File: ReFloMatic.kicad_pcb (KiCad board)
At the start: 2 copper layers, 39 parts, among them CON2 MicroSD_Card, P1 PROG, P2 THERMOCOUPLE, P3 DOOR_SERVO, P4 OVEN, P5 USB_B, Q1 MMUN2211, Q2 MMUN2111, Q3 MMUN2111, Q4 MMUN2211, U1 STM32F030C, U2 MAX31855KASA

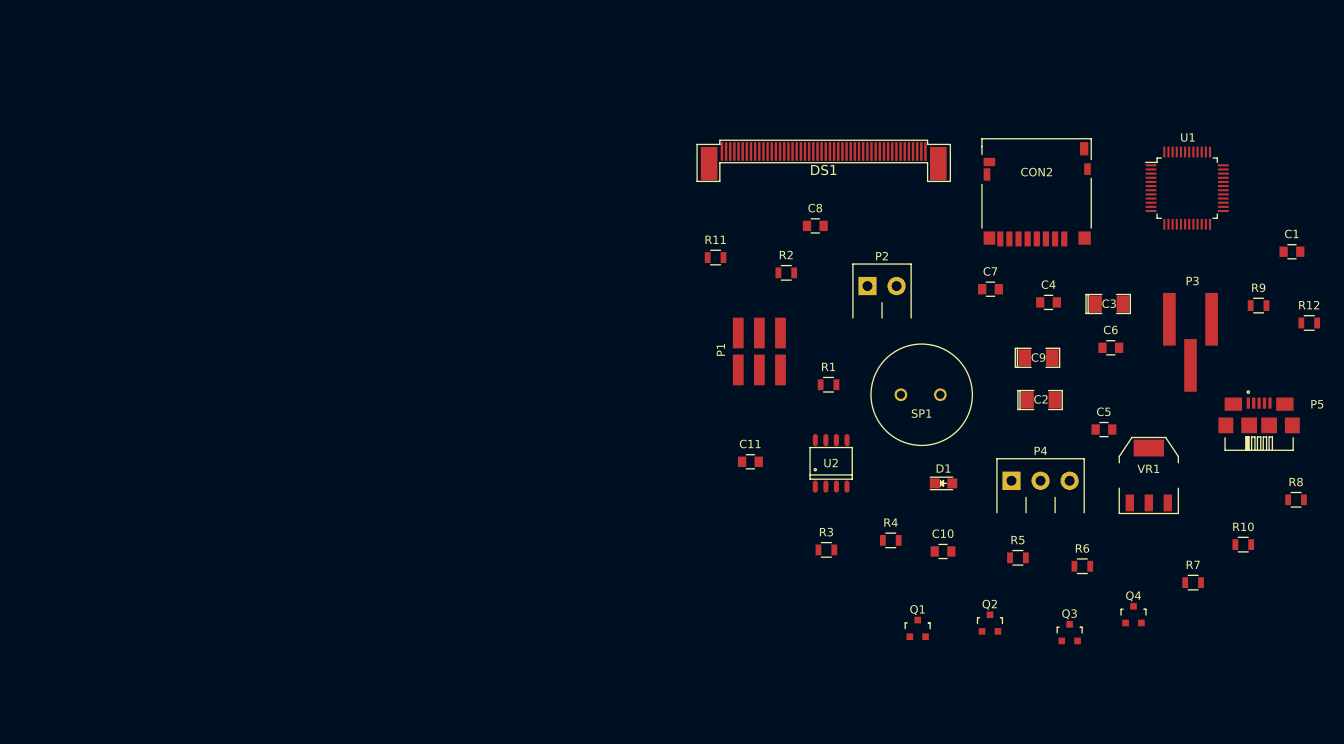
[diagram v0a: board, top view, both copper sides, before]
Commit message: Added TFT footprint that contains display and PCB cutout.
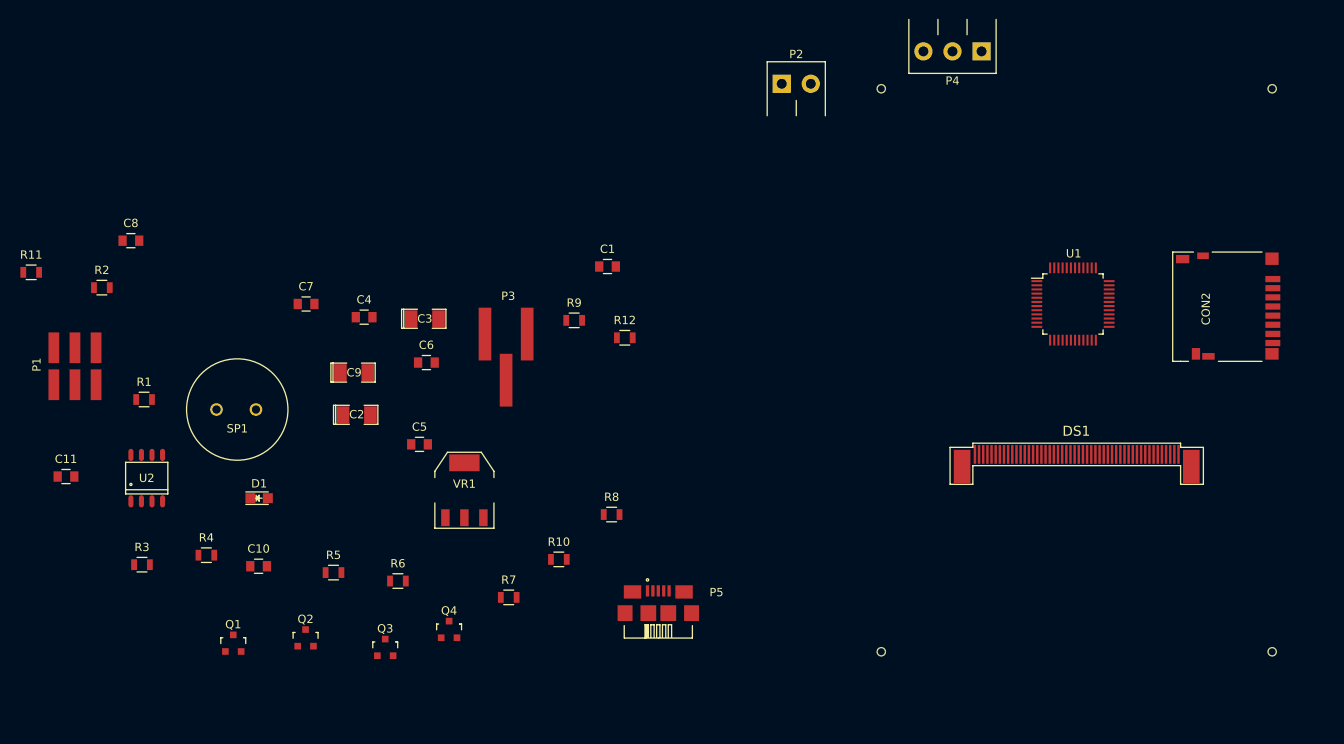
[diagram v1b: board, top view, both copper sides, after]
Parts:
- DS1: footprint TFT:FPC_50 -> TFT:ER-TFT028-4
- moved C4 82.4 mm to (67.5, 99.2)
- moved C6 82.4 mm to (75.0, 104.6)
- moved C9 82.4 mm to (66.3, 105.9)
- moved Q3 82.4 mm to (70.0, 138.9)
- moved R10 82.4 mm to (90.9, 128.3)
- moved R12 82.4 mm to (98.9, 101.7)
- moved R6 82.4 mm to (71.6, 130.9)
- moved R8 82.4 mm to (97.3, 122.9)
- moved R9 82.4 mm to (92.8, 99.6)
- moved VR1 82.4 mm to (79.6, 120.0)
- moved C10 82.4 mm to (54.8, 129.2)
- moved C11 82.4 mm to (31.6, 118.4)
- moved C2 82.4 mm to (66.6, 110.9)
- moved C3 82.4 mm to (74.8, 99.4)
- moved C5 82.4 mm to (74.2, 114.5)
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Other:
- net class Default: clearance 0.2 -> 0.1524; trace_width 0.25 -> 0.1524; via_dia 0.6 -> 0.6858; via_drill 0.4 -> 0.3302
- rule trace_clearance: 0.2 -> 0.1524
- rule trace_min: 0.2 -> 0.1524
- rule via_min_drill: 0.3 -> 0.3302
- rule via_min_size: 0.4 -> 0.6858

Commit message: Preliminary component placement.
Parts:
- added P6: PWR_CONN, Pin_Headers:Pin_Header_Straight_1x02, F.Cu at (153.5, 144.7)
- added REF**: MountingHole_3mm, Mounting_Holes:MountingHole_3mm, F.Cu at (176.5, 144.9)
- added REF**: MountingHole_3mm, Mounting_Holes:MountingHole_3mm, F.Cu at (129.9, 144.7)
- added REF**: MountingHole_3mm, Mounting_Holes:MountingHole_3mm, F.Cu at (129.9, 66.8)
- added REF**: MountingHole_3mm, Mounting_Holes:MountingHole_3mm, F.Cu at (176.5, 66.8)
- P3: footprint Connectors-Custom3:HEADER_1X3_SMD -> Pin_Headers:Pin_Header_Straight_1x03
- moved R11 149.6 mm to (177.0, 93.3)
- moved R2 139.7 mm to (174.0, 74.7)
- moved R1 132.6 mm to (169.1, 74.9)
- moved C11 132.0 mm to (163.6, 120.7), turned to 270 degrees
- moved U2 131.9 mm to (168.4, 83.3), turned to 180 degrees
- moved P1 126.3 mm to (157.3, 85.0), turned to 180 degrees
- moved D1 116.7 mm to (171.0, 132.5), turned to 180 degrees
- moved R3 107.6 mm to (140.4, 88.4)
- moved C10 106.8 mm to (161.2, 120.7), turned to 270 degrees
- moved R4 106.0 mm to (141.0, 76.0)
- moved C8 103.8 mm to (141.2, 110.4)
- moved Q3 103.3 mm to (150.8, 74.6)
- moved Q2 102.5 mm to (144.6, 79.1)
- moved R5 99.4 mm to (145.6, 73.3)
- moved C7 95.4 mm to (155.4, 106.9)
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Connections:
- VR1 pad 4: (no net) -> +3V3
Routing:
- added copper zone on F.Cu, net +3V3
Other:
- board outline added: 54.4 x 85.3 mm

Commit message: Began routing.
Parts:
- added REF**11111: VIA-27mil, Miscellanious:VIA-27mil, F.Cu at (144.9, 139.9)
- added REF**11111: VIA-27mil, Miscellanious:VIA-27mil, F.Cu at (153.3, 138.9)
- added REF**11112: VIA-27mil, Miscellanious:VIA-27mil, F.Cu at (144.9, 140.9)
- added REF**11112: VIA-27mil, Miscellanious:VIA-27mil, F.Cu at (153.3, 140.0)
- added REF**11113: VIA-27mil, Miscellanious:VIA-27mil, F.Cu at (144.9, 142.0)
- added REF**11113: VIA-27mil, Miscellanious:VIA-27mil, F.Cu at (153.3, 141.0)
- added REF**11114: VIA-27mil, Miscellanious:VIA-27mil, F.Cu at (144.9, 143.0)
- added REF**11114: VIA-27mil, Miscellanious:VIA-27mil, F.Cu at (153.3, 142.0)
- added REF**11121: VIA-27mil, Miscellanious:VIA-27mil, F.Cu at (145.9, 139.9)
- added REF**11121: VIA-27mil, Miscellanious:VIA-27mil, F.Cu at (154.3, 138.9)
- added REF**11122: VIA-27mil, Miscellanious:VIA-27mil, F.Cu at (145.9, 140.9)
- added REF**11122: VIA-27mil, Miscellanious:VIA-27mil, F.Cu at (154.3, 140.0)
- added REF**11123: VIA-27mil, Miscellanious:VIA-27mil, F.Cu at (145.9, 142.0)
- added REF**11123: VIA-27mil, Miscellanious:VIA-27mil, F.Cu at (154.3, 141.0)
- added REF**11124: VIA-27mil, Miscellanious:VIA-27mil, F.Cu at (145.9, 143.0)
- added REF**11124: VIA-27mil, Miscellanious:VIA-27mil, F.Cu at (154.3, 142.0)
- added REF**11131: VIA-27mil, Miscellanious:VIA-27mil, F.Cu at (146.9, 139.9)
- added REF**11131: VIA-27mil, Miscellanious:VIA-27mil, F.Cu at (155.3, 138.9)
- added REF**11132: VIA-27mil, Miscellanious:VIA-27mil, F.Cu at (146.9, 140.9)
- added REF**11132: VIA-27mil, Miscellanious:VIA-27mil, F.Cu at (155.3, 140.0)
- added REF**11133: VIA-27mil, Miscellanious:VIA-27mil, F.Cu at (146.9, 142.0)
- added REF**11133: VIA-27mil, Miscellanious:VIA-27mil, F.Cu at (155.3, 141.0)
- added REF**11134: VIA-27mil, Miscellanious:VIA-27mil, F.Cu at (146.9, 143.0)
- added REF**11134: VIA-27mil, Miscellanious:VIA-27mil, F.Cu at (155.3, 142.0)
- added REF**11141: VIA-27mil, Miscellanious:VIA-27mil, F.Cu at (148.0, 139.9)
- added REF**11141: VIA-27mil, Miscellanious:VIA-27mil, F.Cu at (156.4, 138.9)
- added REF**11142: VIA-27mil, Miscellanious:VIA-27mil, F.Cu at (148.0, 140.9)
- added REF**11142: VIA-27mil, Miscellanious:VIA-27mil, F.Cu at (156.4, 140.0)
- added REF**11143: VIA-27mil, Miscellanious:VIA-27mil, F.Cu at (148.0, 142.0)
- added REF**11143: VIA-27mil, Miscellanious:VIA-27mil, F.Cu at (156.4, 141.0)
- added REF**11144: VIA-27mil, Miscellanious:VIA-27mil, F.Cu at (148.0, 143.0)
- added REF**11144: VIA-27mil, Miscellanious:VIA-27mil, F.Cu at (156.4, 142.0)
- moved C6 22.2 mm to (135.7, 103.2), turned to 180 degrees
- moved C4 20.4 mm to (141.8, 110.9), turned to 270 degrees
- moved C5 20.1 mm to (139.5, 110.9), turned to 270 degrees
- moved R2 12.9 mm to (161.2, 73.1), turned to 90 degrees
- moved C8 11.0 mm to (135.6, 100.9), turned to 180 degrees
- moved Q3 10.7 mm to (140.1, 75.2), turned to 90 degrees
- moved R5 7.09 mm to (138.6, 71.9)
- moved C1 6.76 mm to (169.3, 78.1)
- moved R4 6.36 mm to (146.0, 72.0)
- moved R3 6.36 mm to (134.3, 90.2), turned to 180 degrees
- moved R1 4.49 mm to (165.0, 73.0), turned to 90 degrees
- moved Q2 4.03 mm to (144.9, 75.1)
- moved C7 3.91 mm to (155.4, 103.0)
- moved Q1 3.88 mm to (138.1, 90.8)
- moved P1 2.49 mm to (154.8, 85.1), turned to 0 degrees
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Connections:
- DS1 pad 0: (no net) -> GND
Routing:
- net +3V3: track 0.00 -> 291.3 mm, vias 0 -> 4
- net GND: track 0.00 -> 47.9 mm, vias 0 -> 4
- net +5V: track 0.00 -> 40.6 mm
- net Net-(DS1-Pad5): track 0.00 -> 16.9 mm
- net Net-(C1-Pad2): track 0.00 -> 14.9 mm, vias 0 -> 2
- net Net-(DS1-Pad4): track 0.00 -> 14.3 mm
- net Net-(Q1-Pad3): track 0.00 -> 11.7 mm
- net Net-(DS1-Pad3): track 0.00 -> 11.5 mm
- net Net-(C1-Pad1): track 0.00 -> 10.2 mm
- net Net-(DS1-Pad2): track 0.00 -> 9.81 mm
- net Net-(P4-Pad2): track 0.00 -> 5.64 mm
- net Net-(P4-Pad1): track 0.00 -> 5.56 mm
- net Net-(P2-Pad1): track 0.00 -> 5.02 mm
- net Net-(P2-Pad2): track 0.00 -> 4.97 mm
- net Net-(D1-Pad1): track 0.00 -> 4.85 mm, vias 0 -> 2
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- added copper zone on B.Cu, net GND
- added copper zone on F.Cu, net GND
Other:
- net class Default: clearance 0.1524 -> 0.254; trace_width 0.1524 -> 0.508
- rule trace_clearance: 0.1524 -> 0.254

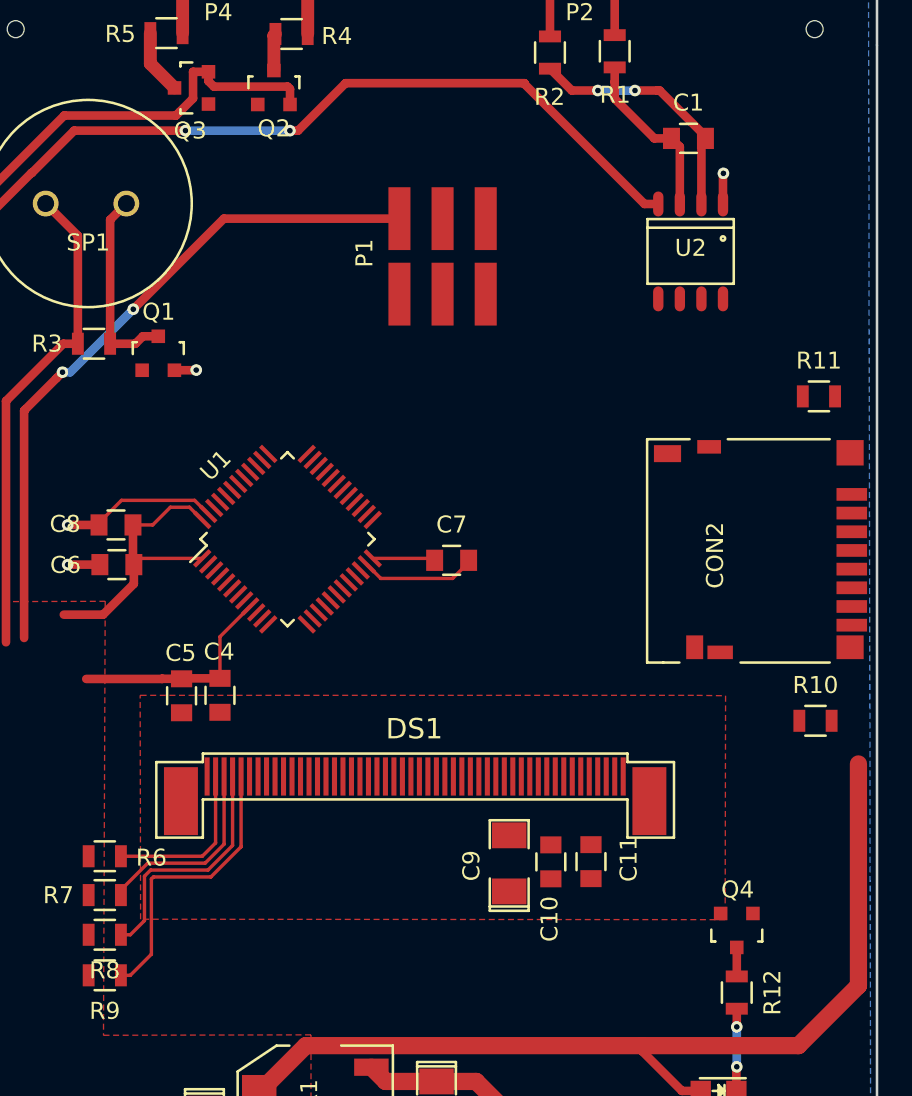
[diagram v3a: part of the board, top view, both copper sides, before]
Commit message: Routing mostly done.  Still need to route TFT traces.
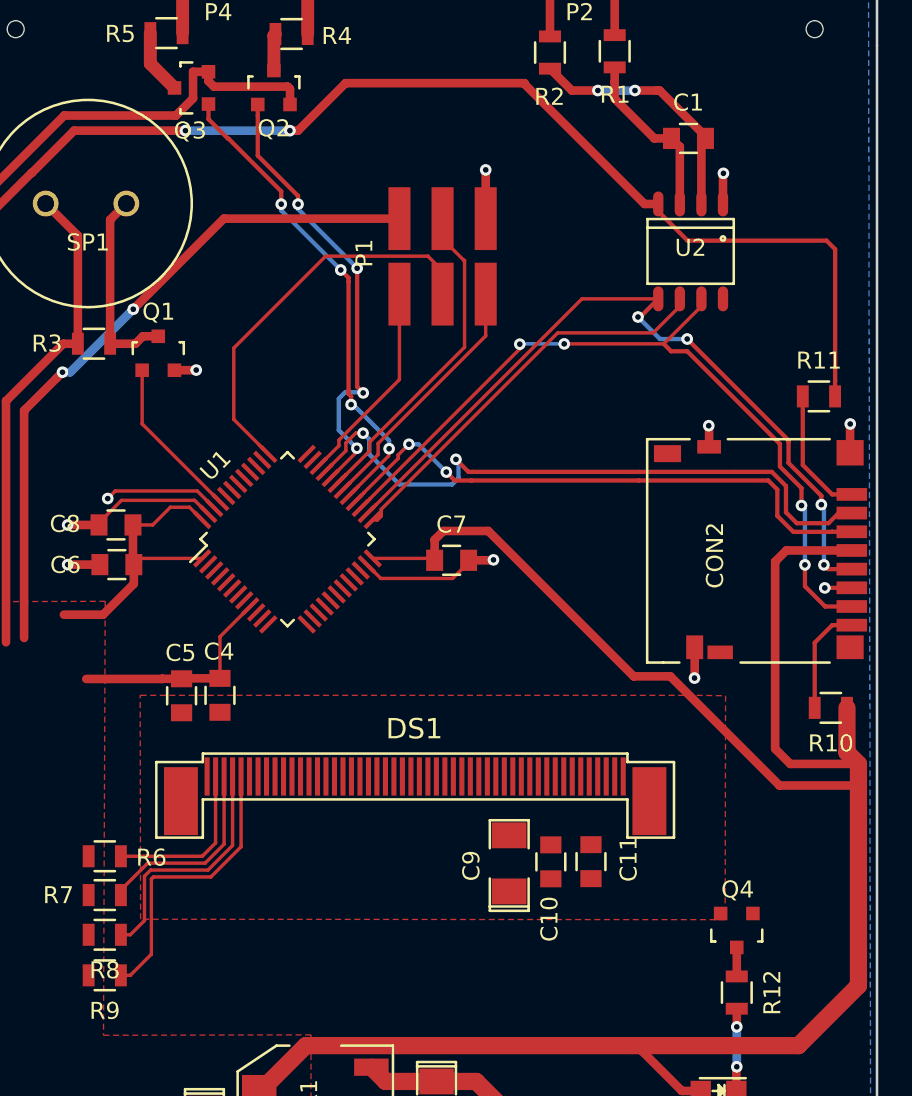
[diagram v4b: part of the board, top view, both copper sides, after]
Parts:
- moved R10 1.18 mm to (177.7, 111.7), turned to 180 degrees
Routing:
- net +3V3: track 291.3 -> 368.9 mm
- net /MAX_SD_MISO: track 0.00 -> 47.1 mm, vias 0 -> 4
- net /MAX_SD_SCK: track 0.00 -> 45.9 mm, vias 0 -> 4
- net /~SD_CS: track 0.00 -> 38.2 mm, vias 0 -> 2
- net /SD_MOSI: track 0.00 -> 33.8 mm, vias 0 -> 2
- net /OVEN2: track 0.00 -> 28.6 mm, vias 0 -> 4
- net /OVEN1: track 0.00 -> 26.9 mm, vias 0 -> 4
- net /~MAX_CS: track 0.00 -> 24.0 mm
- net /SWCLK: track 0.00 -> 23.3 mm
- net /UART_RX: track 0.00 -> 20.1 mm
- net /UART_TX: track 0.00 -> 15.0 mm
- net /SWDIO: track 0.00 -> 12.1 mm
- net GND: track 47.9 -> 58.6 mm, vias 4 -> 10
- net /BUZZER: track 0.00 -> 9.66 mm
- net Net-(CON2-Pad1): track 0.00 -> 7.64 mm
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
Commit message: Finished layout.
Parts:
- added REF**1111111: VIA-27mil, Miscellanious:VIA-27mil, F.Cu at (165.8, 138.4)
- added REF**1111111: VIA-27mil, Miscellanious:VIA-27mil, F.Cu at (138.1, 113.2)
- added REF**1111112: VIA-27mil, Miscellanious:VIA-27mil, F.Cu at (165.8, 139.4)
- added REF**1111112: VIA-27mil, Miscellanious:VIA-27mil, F.Cu at (138.1, 114.2)
- added REF**1111113: VIA-27mil, Miscellanious:VIA-27mil, F.Cu at (165.8, 140.5)
- added REF**1111121: VIA-27mil, Miscellanious:VIA-27mil, F.Cu at (166.8, 138.4)
- added REF**1111121: VIA-27mil, Miscellanious:VIA-27mil, F.Cu at (139.1, 113.2)
- added REF**1111122: VIA-27mil, Miscellanious:VIA-27mil, F.Cu at (166.8, 139.4)
- added REF**1111122: VIA-27mil, Miscellanious:VIA-27mil, F.Cu at (139.1, 114.2)
- added REF**1111123: VIA-27mil, Miscellanious:VIA-27mil, F.Cu at (166.8, 140.5)
- added REF**1111131: VIA-27mil, Miscellanious:VIA-27mil, F.Cu at (167.8, 138.4)
- added REF**1111131: VIA-27mil, Miscellanious:VIA-27mil, F.Cu at (140.2, 113.2)
- added REF**11111311: VIA-27mil, Miscellanious:VIA-27mil, F.Cu at (146.7, 112.0)
- added REF**111113111: VIA-27mil, Miscellanious:VIA-27mil, F.Cu at (165.2, 111.7)
- added REF**1111131111: VIA-27mil, Miscellanious:VIA-27mil, F.Cu at (146.2, 118.7)
- added REF**1111131112: VIA-27mil, Miscellanious:VIA-27mil, F.Cu at (146.2, 119.9)
- added REF**1111131113: VIA-27mil, Miscellanious:VIA-27mil, F.Cu at (146.2, 121.2)
- added REF**1111131114: VIA-27mil, Miscellanious:VIA-27mil, F.Cu at (146.2, 122.5)
- added REF**111113112: VIA-27mil, Miscellanious:VIA-27mil, F.Cu at (165.2, 112.7)
- added REF**1111131121: VIA-27mil, Miscellanious:VIA-27mil, F.Cu at (147.5, 118.7)
- added REF**1111131122: VIA-27mil, Miscellanious:VIA-27mil, F.Cu at (147.5, 119.9)
- added REF**1111131123: VIA-27mil, Miscellanious:VIA-27mil, F.Cu at (147.5, 121.2)
- added REF**1111131124: VIA-27mil, Miscellanious:VIA-27mil, F.Cu at (147.5, 122.5)
- added REF**111113113: VIA-27mil, Miscellanious:VIA-27mil, F.Cu at (165.2, 113.7)
- added REF**1111131131: VIA-27mil, Miscellanious:VIA-27mil, F.Cu at (148.7, 118.7)
- added REF**1111131132: VIA-27mil, Miscellanious:VIA-27mil, F.Cu at (148.7, 119.9)
- added REF**1111131133: VIA-27mil, Miscellanious:VIA-27mil, F.Cu at (148.7, 121.2)
- added REF**1111131134: VIA-27mil, Miscellanious:VIA-27mil, F.Cu at (148.7, 122.5)
- added REF**1111131141: VIA-27mil, Miscellanious:VIA-27mil, F.Cu at (150.0, 118.7)
- added REF**1111131142: VIA-27mil, Miscellanious:VIA-27mil, F.Cu at (150.0, 119.9)
- added REF**1111131143: VIA-27mil, Miscellanious:VIA-27mil, F.Cu at (150.0, 121.2)
- added REF**1111131144: VIA-27mil, Miscellanious:VIA-27mil, F.Cu at (150.0, 122.5)
- added REF**1111131151: VIA-27mil, Miscellanious:VIA-27mil, F.Cu at (151.3, 118.7)
- added REF**1111131152: VIA-27mil, Miscellanious:VIA-27mil, F.Cu at (151.3, 119.9)
- added REF**1111131153: VIA-27mil, Miscellanious:VIA-27mil, F.Cu at (151.3, 121.2)
- added REF**1111131154: VIA-27mil, Miscellanious:VIA-27mil, F.Cu at (151.3, 122.5)
- added REF**1111131161: VIA-27mil, Miscellanious:VIA-27mil, F.Cu at (152.6, 118.7)
- added REF**1111131162: VIA-27mil, Miscellanious:VIA-27mil, F.Cu at (152.6, 119.9)
- added REF**1111131163: VIA-27mil, Miscellanious:VIA-27mil, F.Cu at (152.6, 121.2)
- added REF**1111131164: VIA-27mil, Miscellanious:VIA-27mil, F.Cu at (152.6, 122.5)
- added REF**1111131171: VIA-27mil, Miscellanious:VIA-27mil, F.Cu at (153.8, 118.7)
- added REF**1111131172: VIA-27mil, Miscellanious:VIA-27mil, F.Cu at (153.8, 119.9)
- added REF**1111131173: VIA-27mil, Miscellanious:VIA-27mil, F.Cu at (153.8, 121.2)
- added REF**1111131174: VIA-27mil, Miscellanious:VIA-27mil, F.Cu at (153.8, 122.5)
- added REF**1111131181: VIA-27mil, Miscellanious:VIA-27mil, F.Cu at (155.1, 118.7)
- added REF**1111131182: VIA-27mil, Miscellanious:VIA-27mil, F.Cu at (155.1, 119.9)
- added REF**1111131183: VIA-27mil, Miscellanious:VIA-27mil, F.Cu at (155.1, 121.2)
- added REF**1111131184: VIA-27mil, Miscellanious:VIA-27mil, F.Cu at (155.1, 122.5)
- added REF**1111131191: VIA-27mil, Miscellanious:VIA-27mil, F.Cu at (156.4, 118.7)
- added REF**1111131192: VIA-27mil, Miscellanious:VIA-27mil, F.Cu at (156.4, 119.9)
- added REF**1111131193: VIA-27mil, Miscellanious:VIA-27mil, F.Cu at (156.4, 121.2)
- added REF**1111131194: VIA-27mil, Miscellanious:VIA-27mil, F.Cu at (156.4, 122.5)
- added REF**11111312: VIA-27mil, Miscellanious:VIA-27mil, F.Cu at (146.7, 113.1)
- added REF**111113121: VIA-27mil, Miscellanious:VIA-27mil, F.Cu at (166.2, 111.7)
- added REF**111113122: VIA-27mil, Miscellanious:VIA-27mil, F.Cu at (166.2, 112.7)
- added REF**111113123: VIA-27mil, Miscellanious:VIA-27mil, F.Cu at (166.2, 113.7)
- added REF**111113131: VIA-27mil, Miscellanious:VIA-27mil, F.Cu at (167.3, 111.7)
- added REF**111113132: VIA-27mil, Miscellanious:VIA-27mil, F.Cu at (167.3, 112.7)
- added REF**111113133: VIA-27mil, Miscellanious:VIA-27mil, F.Cu at (167.3, 113.7)
- added REF**1111132: VIA-27mil, Miscellanious:VIA-27mil, F.Cu at (167.8, 139.4)
- added REF**1111132: VIA-27mil, Miscellanious:VIA-27mil, F.Cu at (140.2, 114.2)
- added REF**11111321: VIA-27mil, Miscellanious:VIA-27mil, F.Cu at (147.7, 112.0)
- added REF**11111322: VIA-27mil, Miscellanious:VIA-27mil, F.Cu at (147.7, 113.1)
- added REF**1111133: VIA-27mil, Miscellanious:VIA-27mil, F.Cu at (167.8, 140.5)
- added REF**1111141: VIA-27mil, Miscellanious:VIA-27mil, F.Cu at (168.8, 138.4)
- added REF**1111142: VIA-27mil, Miscellanious:VIA-27mil, F.Cu at (168.8, 139.4)
- added REF**1111143: VIA-27mil, Miscellanious:VIA-27mil, F.Cu at (168.8, 140.5)
- added REF**1111151: VIA-27mil, Miscellanious:VIA-27mil, F.Cu at (169.8, 138.4)
- added REF**1111152: VIA-27mil, Miscellanious:VIA-27mil, F.Cu at (169.8, 139.4)
- added REF**1111153: VIA-27mil, Miscellanious:VIA-27mil, F.Cu at (169.8, 140.5)
- added REF**1111161: VIA-27mil, Miscellanious:VIA-27mil, F.Cu at (170.8, 138.4)
- added REF**1111162: VIA-27mil, Miscellanious:VIA-27mil, F.Cu at (170.8, 139.4)
- added REF**1111163: VIA-27mil, Miscellanious:VIA-27mil, F.Cu at (170.8, 140.5)
- moved C11 12.2 mm to (175.7, 119.2)
- moved C10 12.0 mm to (173.1, 119.1)
- moved C9 11.6 mm to (170.3, 119.0)
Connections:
- P5 pad : (no net) -> GND
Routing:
- net +3V3: track 368.9 -> 438.7 mm
- net GND: track 58.6 -> 126.4 mm, vias 10 -> 12
- net /SERVO_PWM: track 6.87 -> 53.4 mm, vias 1 -> 3
- net /STATUS: track 0.00 -> 45.2 mm, vias 0 -> 4
- net /TFT_TP_X+: track 0.00 -> 29.9 mm, vias 0 -> 2
- net /TFT_TP_Y+: track 0.00 -> 29.8 mm, vias 0 -> 2
- net /TFT_TP_X-: track 0.00 -> 27.9 mm, vias 0 -> 2
- net /TFT_TP_Y-: track 0.00 -> 24.7 mm, vias 0 -> 2
- net /~TFT_CS: track 0.00 -> 19.7 mm, vias 0 -> 2
- net /TFT_SCK: track 0.00 -> 18.7 mm, vias 0 -> 2
- net /TFT_WR: track 0.00 -> 16.6 mm
- net /TFT_MOSI: track 0.00 -> 15.0 mm
- net /TFT_MISO: track 0.00 -> 14.7 mm
- net /~TFT_RS: track 0.00 -> 13.7 mm, vias 0 -> 2
- net +5V: track 40.6 -> 49.8 mm
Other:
- net class Default: clearance 0.254 -> 0.1524; trace_width 0.508 -> 0.1524
- rule trace_clearance: 0.254 -> 0.1524

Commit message: Added logo.
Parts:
- added G***: RE-FLO-MATIC_LOGO, Logos:RE-FLO-MATIC_LOGO, F.Cu at (157.7, 92.2)
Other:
- board text added: "By R. Angeli"
- board text added: "Rev. A"

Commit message: Finished PCB layout. Generated gerbers.
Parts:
- added DS1: ER-TFT028-4, TFT:ER-TFT028-4, F.Cu at (153.2, 115.7)
- moved G*** 2.22 mm to (157.5, 94.4)
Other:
- board text added: "+5V"
- board text added: "3V3"
- board text added: "CLK"
- board text added: "DIO"
- board text added: "GND"
- board text added: "OVEN1"
- board text added: "OVEN2"
- board text added: "PWM"
- board text added: "RX"
- board text added: "T+"
- board text added: "T-"
- board text added: "TX"
